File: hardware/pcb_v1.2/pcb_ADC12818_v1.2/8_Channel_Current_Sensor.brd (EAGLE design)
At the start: 44 parts, among them Q1 BSS138, Q2 BSS138, SW1 DIP-SLIDE-SWITCH-EG1218

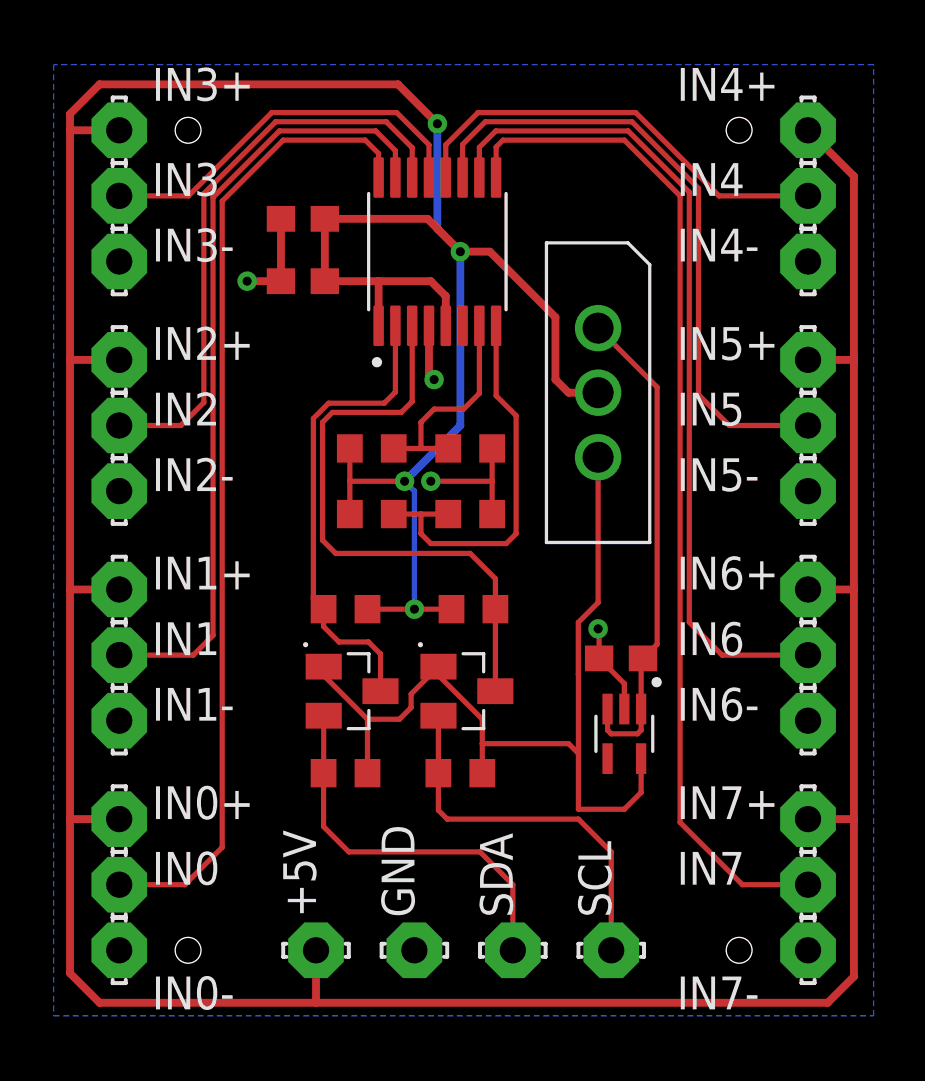
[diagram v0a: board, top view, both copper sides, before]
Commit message: New PCB designs, reorganized files, removed clutter
Added pcb v1.2 the final draft of the ADC12818 board.
Added pcb v2.0 the new board boased on the MAX1614EE+ ADC
Added datasheet for MAX ADC
Renamed folders to have consistent naming scheme
Removed unncessary tempoary files
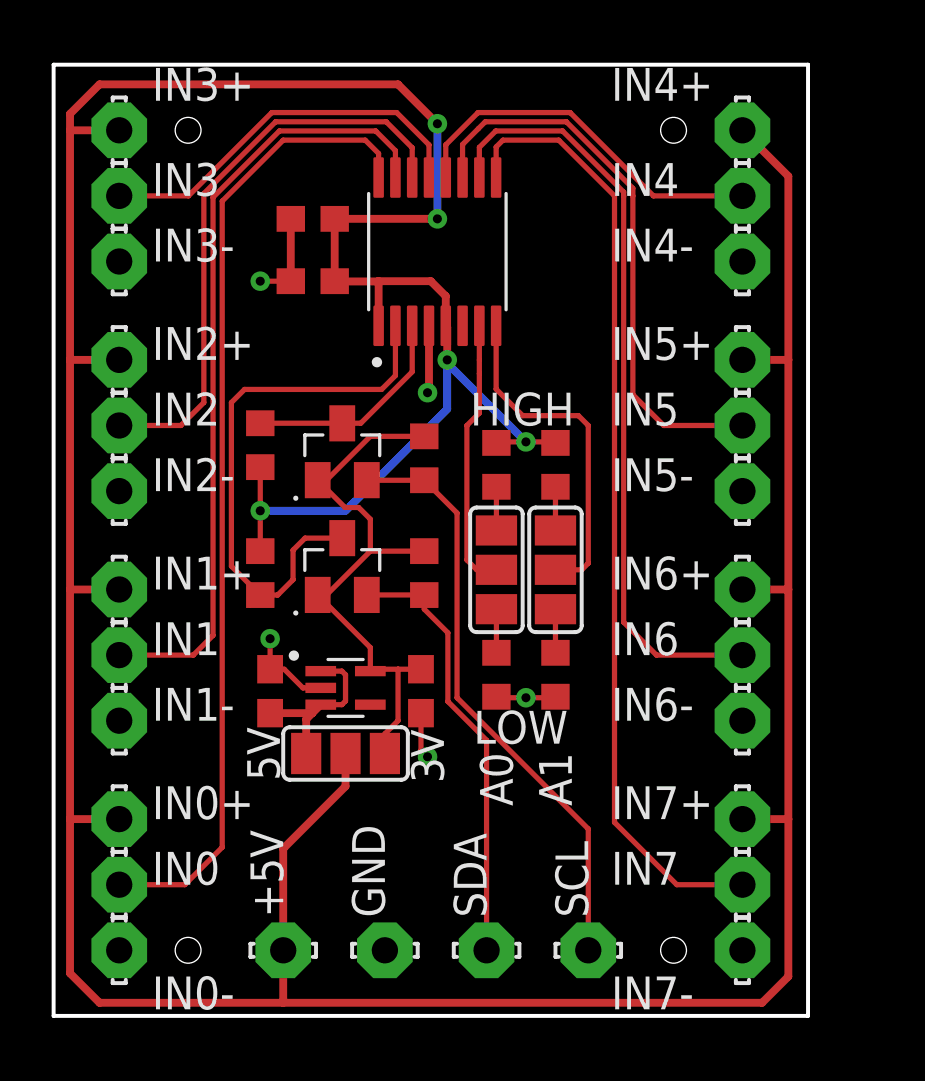
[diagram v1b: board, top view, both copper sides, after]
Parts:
- removed SW1: DIP-SLIDE-SWITCH-EG1218, EG1218-DIP-SLIDE-SWITCH:SW3-2.5-11.6X4.0X5.4+2.0MM
- added +5V_JUMP, A0_JUMP, A1_JUMP: (no value), jumper:SJ_2
- added C3: 1uF, resistor:C0603
- moved C5 13.6 mm to (8.38, 12.6), turned to 90 degrees
- moved R5 12.3 mm to (14.4, 21.6), turned to 90 degrees
- moved REG 10.9 mm to (11.3, 12.7), turned to 270 degrees
- moved Q1 10.5 mm to (11.2, 21.8), turned to 0 degrees
- moved R7 10.4 mm to (8.00, 22.1), turned to 90 degrees
- moved R2 8.82 mm to (17.1, 13.2), turned to 90 degrees
- moved R6 8.33 mm to (14.4, 17.1), turned to 90 degrees
- moved R3 7.36 mm to (19.4, 21.3), turned to 90 degrees
- moved R4 7.04 mm to (19.4, 13.2), turned to 90 degrees
- moved R1 4.87 mm to (17.1, 21.3), turned to 90 degrees
- moved Q2 4.84 mm to (11.2, 17.4), turned to 0 degrees
- moved R8 3.59 mm to (8.00, 17.1), turned to 270 degrees
- moved IN4 2.54 mm to (26.7, 31.8)
- moved IN4+ 2.54 mm to (26.7, 34.3)
- moved IN4- 2.54 mm to (26.7, 29.2)
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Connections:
- removed net +5V-S: C5.1, REG.1, REG.3, SW1.1
- new net +5V-R: +5V_JUMP.3, C5.1, REG.1, REG.3
- new net N$1: A1_JUMP.3, R3.1
- new net N$2: A1_JUMP.1, R4.2
- new net N$3: A0_JUMP.1, R2.2
- new net N$4: A0_JUMP.3, R1.1
- net +5V: now also +5V_JUMP.2; no longer SW1.2
- net A0: now also A0_JUMP.2; no longer R1.1, R2.2
- net A1: now also A1_JUMP.2; no longer R3.1, R4.2
- net GND: now also C3.2
- net V-PU: now also +5V_JUMP.1, C3.1; no longer SW1.3
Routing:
- net +5V-S: track 19.1 -> 0.00 mm
- net SCL5: track 23.0 -> 8.50 mm
- net V-PU: track 35.5 -> 22.9 mm
- net SCL: track 14.8 -> 23.1 mm
- net +5V: track 182.1 -> 173.9 mm, vias 4 -> 5
- net +5V-R: track 0.00 -> 6.91 mm
- net SDA5: track 18.5 -> 22.0 mm
- net IN7: track 39.5 -> 37.0 mm
- net IN6: track 32.3 -> 29.8 mm
- net IN5: track 24.6 -> 22.0 mm
- net IN4: track 17.1 -> 14.6 mm
- net A0: track 8.50 -> 10.6 mm
- net A1: track 15.2 -> 13.3 mm
- net SDA: track 15.1 -> 17.0 mm
- net N$4: track 0.00 -> 1.69 mm
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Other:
- board outline added: 29.2 x 36.8 mm
- board text added: "3V"
- board text added: "5V"
- board text added: "A0"
- board text added: "A1"
- board text added: "HIGH"
- board text added: "LOW"
